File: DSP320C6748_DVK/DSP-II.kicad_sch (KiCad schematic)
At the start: 3 parts, among them IC8 SN74LVC1G11DBVR, U1 TMS320C6748EZWT4

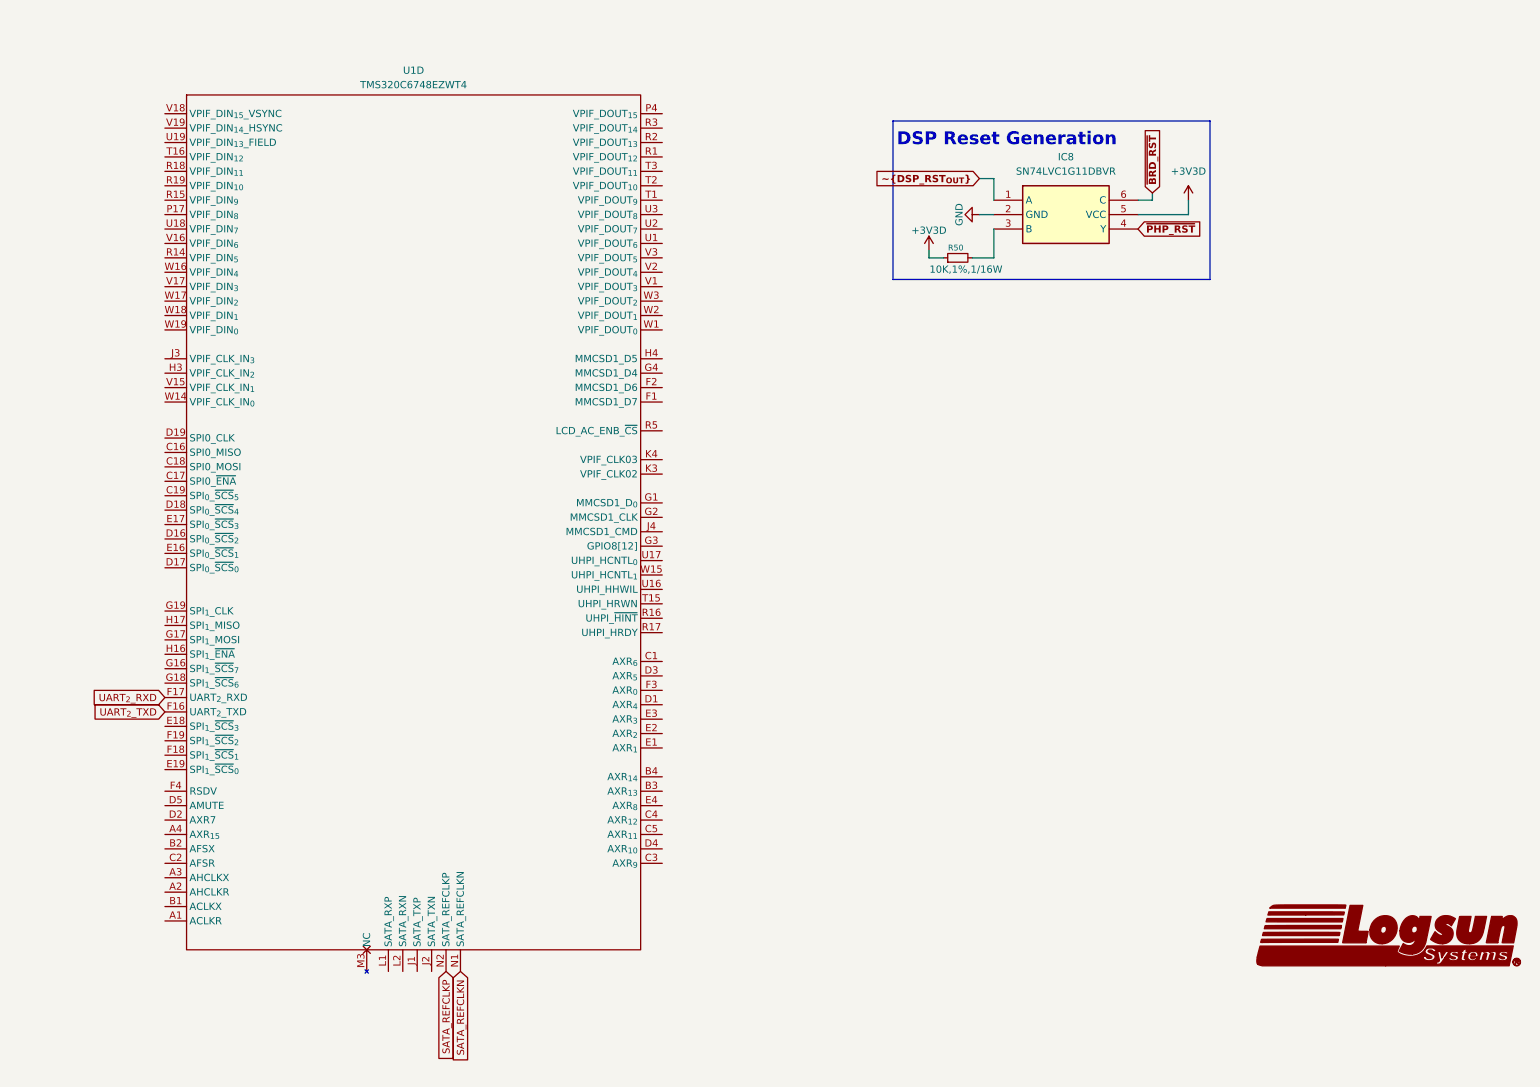
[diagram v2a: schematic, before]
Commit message: Partial VGA-LCD schematic added
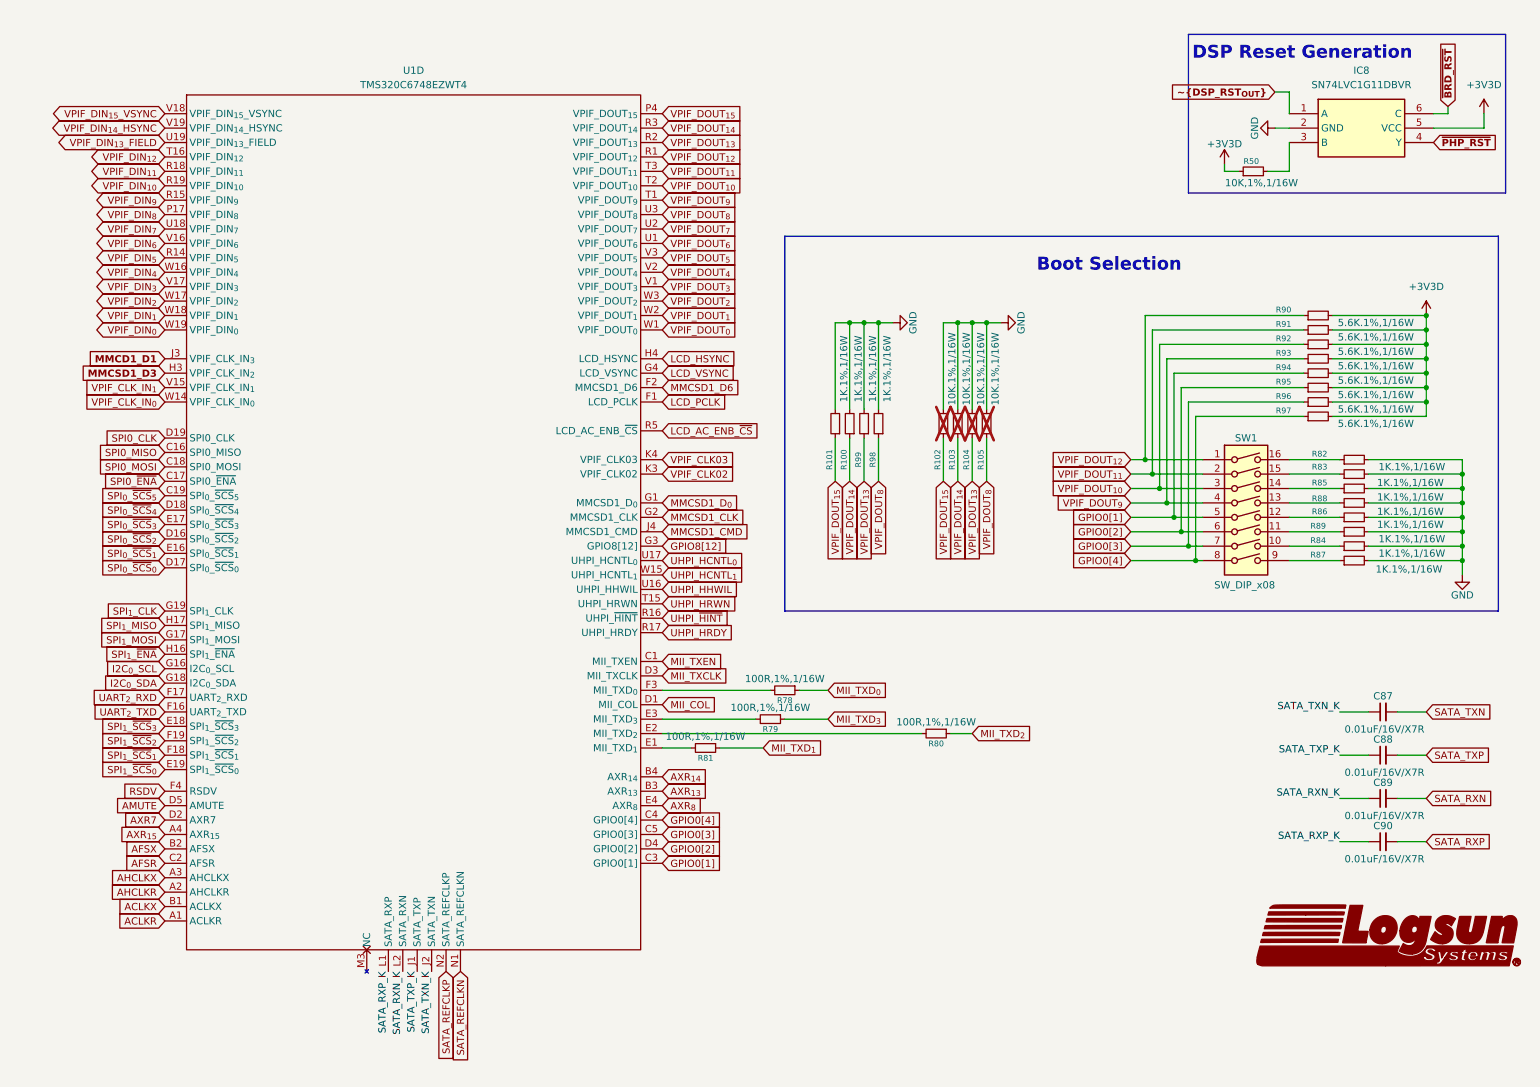
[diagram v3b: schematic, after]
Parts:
- added C87, C88, C89, C90: 0.01uF/16V/X7R, symbol Device:C_Small
- added R100, R101, R82, R83, R84, R85, R86, R87, R88, R89, R98, R99: 1K.1%,1/16W, symbol Device:R_Small
- added R102, R103, R104, R105: 10K.1%,1/16W, symbol Device:R_Small
- added R78, R79, R80, R81: 100R,1%,1/16W, symbol Device:R_Small
- added R90, R91, R92, R93, R94, R95, R96, R97: 5.6K.1%,1/16W, symbol Device:R_Small
- added SW1: SW_DIP_x08, symbol Switch:SW_DIP_x08
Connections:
- net +3V3D: now also R90.2, R91.2, R92.2, R93.2, R94.2, R95.2, R96.2, R97.2
- net GND: now also R100.2, R101.2, R102.2, R103.2, R104.2, R105.2, R82.2, R83.2, R84.2, R85.2, R86.2, R87.2, R88.2, R89.2, R98.2, R99.2
- net ACLKR: now reaches U1.A1 (ACLKR)
- net AHCLKR: now reaches U1.A2 (AHCLKR)
- net AHCLKX: now reaches U1.A3 (AHCLKX)
- net AXR_{15}: now reaches U1.A4 (AXR_{15})
- net ACLKX: now reaches U1.B1 (ACLKX)
- net AFSX: now reaches U1.B2 (AFSX)
- net AXR_{13}: now reaches U1.B3 (AXR_{13})
- net AXR_{14}: now reaches U1.B4 (AXR_{14})
- net MII_TXEN: now reaches U1.C1 (AXR_{6})
- net SPI0_MISO: now reaches U1.C16 (SPI0_MISO)
- net SPI0_~{ENA}: now reaches U1.C17 (SPI0_~{ENA})
- net SPI0_MOSI: now reaches U1.C18 (SPI0_MOSI)
- net SPI_{0}_~{SCS}_{5}: now reaches U1.C19 (SPI_{0}_~{SCS}_{5})
- net AFSR: now reaches U1.C2 (AFSR)
- net GPIO0[1]: now reaches U1.C3 (AXR_{9})
- net GPIO0[1]: now also R94.1, SW1.5
- net GPIO0[4]: now reaches U1.C4 (AXR_{12})
- net GPIO0[4]: now also R97.1, SW1.8
- net GPIO0[3]: now reaches U1.C5 (AXR_{11})
- net GPIO0[3]: now also R96.1, SW1.7
- net MII_COL: now reaches U1.D1 (AXR_{4})
- net SPI_{0}_~{SCS}_{2}: now reaches U1.D16 (SPI_{0}_~{SCS}_{2})
- net SPI_{0}_~{SCS}_{0}: now reaches U1.D17 (SPI_{0}_~{SCS}_{0})
- net SPI_{0}_~{SCS}_{4}: now reaches U1.D18 (SPI_{0}_~{SCS}_{4})
- net SPI0_CLK: now reaches U1.D19 (SPI0_CLK)
- net AXR7: now reaches U1.D2 (AXR7)
- net MII_TXCLK: now reaches U1.D3 (AXR_{5})
- net GPIO0[2]: now reaches U1.D4 (AXR_{10})
- net GPIO0[2]: now also R95.1, SW1.6
- net AMUTE: now reaches U1.D5 (AMUTE)
- net at U1.E1 (AXR_{1}): now also R81.2
- net SPI_{0}_~{SCS}_{1}: now reaches U1.E16 (SPI_{0}_~{SCS}_{1})
- net SPI_{0}_~{SCS}_{3}: now reaches U1.E17 (SPI_{0}_~{SCS}_{3})
- net SPI_{1}_~{SCS}_{3}: now reaches U1.E18 (SPI_{1}_~{SCS}_{3})
- net SPI_{1}_~{SCS}_{0}: now reaches U1.E19 (SPI_{1}_~{SCS}_{0})
- net at U1.E2 (AXR_{2}): now also R80.2
- net at U1.E3 (AXR_{3}): now also R79.2
- net AXR_{8}: now reaches U1.E4 (AXR_{8})
- net LCD_PCLK: now reaches U1.F1 (MMCSD1_D7)
- net SPI_{1}_~{SCS}_{1}: now reaches U1.F18 (SPI_{1}_~{SCS}_{1})
- net SPI_{1}_~{SCS}_{2}: now reaches U1.F19 (SPI_{1}_~{SCS}_{2})
- net MMCSD1_D6: now reaches U1.F2 (MMCSD1_D6)
- net at U1.F3 (AXR_{0}): now also R78.2
- net RSDV: now reaches U1.F4 (RSDV)
- net MMCSD1_D_{0}: now reaches U1.G1 (MMCSD1_D_{0})
- net I2C_{0}_SCL: now reaches U1.G16 (SPI_{1}_~{SCS}_{7})
- net SPI_{1}_MOSI: now reaches U1.G17 (SPI_{1}_MOSI)
- net I2C_{0}_SDA: now reaches U1.G18 (SPI_{1}_~{SCS}_{6})
- net SPI_{1}_CLK: now reaches U1.G19 (SPI_{1}_CLK)
- net MMCSD1_CLK: now reaches U1.G2 (MMCSD1_CLK)
- net GPIO8[12]: now reaches U1.G3 (GPIO8[12])
- net LCD_VSYNC: now reaches U1.G4 (MMCSD1_D4)
- net SPI_{1}_~{ENA}: now reaches U1.H16 (SPI_{1}_~{ENA})
- net SPI_{1}_MISO: now reaches U1.H17 (SPI_{1}_MISO)
- net MMCSD1_D3: now reaches U1.H3 (VPIF_CLK_IN_{2})
- net LCD_HSYNC: now reaches U1.H4 (MMCSD1_D5)
- net SATA_TXP_K: now reaches U1.J1 (SATA_TXP)
- net SATA_TXP_K: now also C88.1
- net SATA_TXN_K: now reaches U1.J2 (SATA_TXN)
- net SATA_TXN_K: now also C87.1
- net MMCD1_D1: now reaches U1.J3 (VPIF_CLK_IN_{3})
- net MMCSD1_CMD: now reaches U1.J4 (MMCSD1_CMD)
- net VPIF_CLK02: now reaches U1.K3 (VPIF_CLK02)
- net VPIF_CLK03: now reaches U1.K4 (VPIF_CLK03)
- net SATA_RXP_K: now reaches U1.L1 (SATA_RXP)
- net SATA_RXP_K: now also C90.1
- net SATA_RXN_K: now reaches U1.L2 (SATA_RXN)
- net SATA_RXN_K: now also C89.1
- net VPIF_DIN_{8}: now reaches U1.P17 (VPIF_DIN_{8})
- net VPIF_DOUT_{15}: now reaches U1.P4 (VPIF_DOUT_{15})
- net VPIF_DOUT_{15}: now also R101.1, R102.1
- net VPIF_DOUT_{12}: now reaches U1.R1 (VPIF_DOUT_{12})
- net VPIF_DOUT_{12}: now also R90.1, SW1.1
- net VPIF_DIN_{5}: now reaches U1.R14 (VPIF_DIN_{5})
- net VPIF_DIN_{9}: now reaches U1.R15 (VPIF_DIN_{9})
- net UHPI_~{HINT}: now reaches U1.R16 (UHPI_~{HINT})
- net UHPI_HRDY: now reaches U1.R17 (UHPI_HRDY)
- net VPIF_DIN_{11}: now reaches U1.R18 (VPIF_DIN_{11})
- net VPIF_DIN_{10}: now reaches U1.R19 (VPIF_DIN_{10})
- net VPIF_DOUT_{13}: now reaches U1.R2 (VPIF_DOUT_{13})
- net VPIF_DOUT_{13}: now also R104.1, R99.1
- net VPIF_DOUT_{14}: now reaches U1.R3 (VPIF_DOUT_{14})
- net VPIF_DOUT_{14}: now also R100.1, R103.1
- net LCD_AC_ENB_~{CS}: now reaches U1.R5 (LCD_AC_ENB_~{CS})
- net VPIF_DOUT_{9}: now reaches U1.T1 (VPIF_DOUT_{9})
- net VPIF_DOUT_{9}: now also R93.1, SW1.4
- net UHPI_HRWN: now reaches U1.T15 (UHPI_HRWN)
- net VPIF_DIN_{12}: now reaches U1.T16 (VPIF_DIN_{12})
- net VPIF_DOUT_{10}: now reaches U1.T2 (VPIF_DOUT_{10})
- net VPIF_DOUT_{10}: now also R92.1, SW1.3
- net VPIF_DOUT_{11}: now reaches U1.T3 (VPIF_DOUT_{11})
- net VPIF_DOUT_{11}: now also R91.1, SW1.2
- net VPIF_DOUT_{6}: now reaches U1.U1 (VPIF_DOUT_{6})
- net UHPI_HHWIL: now reaches U1.U16 (UHPI_HHWIL)
- net UHPI_HCNTL_{0}: now reaches U1.U17 (UHPI_HCNTL_{0})
- net VPIF_DIN_{7}: now reaches U1.U18 (VPIF_DIN_{7})
- net VPIF_DIN_{13}_FIELD: now reaches U1.U19 (VPIF_DIN_{13}_FIELD)
- net VPIF_DOUT_{7}: now reaches U1.U2 (VPIF_DOUT_{7})
- net VPIF_DOUT_{8}: now reaches U1.U3 (VPIF_DOUT_{8})
- net VPIF_DOUT_{8}: now also R105.1, R98.1
- net VPIF_DOUT_{3}: now reaches U1.V1 (VPIF_DOUT_{3})
- net VPIF_CLK_IN_{1}: now reaches U1.V15 (VPIF_CLK_IN_{1})
- net VPIF_DIN_{6}: now reaches U1.V16 (VPIF_DIN_{6})
- net VPIF_DIN_{3}: now reaches U1.V17 (VPIF_DIN_{3})
- net VPIF_DIN_{15}_VSYNC: now reaches U1.V18 (VPIF_DIN_{15}_VSYNC)
- net VPIF_DIN_{14}_HSYNC: now reaches U1.V19 (VPIF_DIN_{14}_HSYNC)
- net VPIF_DOUT_{4}: now reaches U1.V2 (VPIF_DOUT_{4})
- net VPIF_DOUT_{5}: now reaches U1.V3 (VPIF_DOUT_{5})
- net VPIF_DOUT_{0}: now reaches U1.W1 (VPIF_DOUT_{0})
- net VPIF_CLK_IN_{0}: now reaches U1.W14 (VPIF_CLK_IN_{0})
- net UHPI_HCNTL_{1}: now reaches U1.W15 (UHPI_HCNTL_{1})
- net VPIF_DIN_{4}: now reaches U1.W16 (VPIF_DIN_{4})
- net VPIF_DIN_{2}: now reaches U1.W17 (VPIF_DIN_{2})
- net VPIF_DIN_{1}: now reaches U1.W18 (VPIF_DIN_{1})
- net VPIF_DIN_{0}: now reaches U1.W19 (VPIF_DIN_{0})
- net VPIF_DOUT_{1}: now reaches U1.W2 (VPIF_DOUT_{1})
- net VPIF_DOUT_{2}: now reaches U1.W3 (VPIF_DOUT_{2})
- new net: R83.1, SW1.15
- new net: R85.1, SW1.14
- new net: R84.1, SW1.10
- new net: R89.1, SW1.11
- new net: R86.1, SW1.12
- new net: R88.1, SW1.13
- new net: R82.1, SW1.16
- new net: R87.1, SW1.9
- new net MII_TXD_{0}: R78.1
- new net MII_TXD_{1}: R81.1
- new net MII_TXD_{2}: R80.1
- new net MII_TXD_{3}: R79.1
- new net SATA_RXN: C89.2
- new net SATA_RXP: C90.2
- new net SATA_TXN: C87.2
- new net SATA_TXP: C88.2
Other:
- note added: "Boot Selection"
- moved on the sheet: IC8, R50

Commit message: LCD Schematic Completed
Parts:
- added D8, D9: LED_RED, symbol Device:LED_Small
- added IC10, IC11: MUN5211DW1T1G, SOT65P210X110-6N, symbol MUN5211DW1T1G:MUN5211DW1T1G
- added R112: 0R,5%,1/10W, symbol Device:R_Small
- added R113, R114, R115, R116: 10K,1%,1/16W, symbol Device:R_Small
- added R117, R118: 33R,5%,1/16W, symbol Device:R_Small
- added R119, R122: 330R,5%,1/16W, symbol Device:R_Small
- added R120, R121: 100K,5%,1/16W, symbol Device:R_Small
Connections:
- net +3V3D: now also R113.2, R114.2, R115.2, R116.2, R119.1, R122.1
- net ACLKX: now also R117.1
- net AFSX: now also R118.1
- net GND: now also IC10.1 (E2), IC11.1 (E2), R120.2, R121.2
- net I2C_{0}_SCL: now also R113.1
- net I2C_{0}_SDA: now also R114.1
- net UART_{2}_RXD: now also R115.1
- net UART_{2}_TXD: now also R116.1
- net VPIF_CLK_IN_{1}: now also R112.2
- net UHPI_HRDY renamed GPIO6[13]
- net GPIO6[13]: now also IC10.2 (B2), R120.1
- net UHPI_~{HINT} renamed GPIO6[12]
- net GPIO6[12]: now also IC11.2 (B2), R121.1
- net VPIF_CLK_IN_{0} renamed CAM_CLK
- net CAM_CLK: now also R112.1
- new net: D9.1 (K), IC11.6 (C2)
- new net: D9.2 (A), R122.2
- new net: D8.2 (A), R119.2
- new net: D8.1 (K), IC10.6 (C2)
- new net AIC_BCLK: R117.2
- new net AIC_WCLK: R118.2
- no-connect marks 0 -> 6
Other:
- note added: "0111"
- note added: "1010"
- note added: "Bits"
- note added: "Device"
- note added: "NAND Flash"
- note added: "UART2"
- moved on the sheet: R100, R101, R102, R103, R104, R105, R78, R79, R80, R81, R82, R83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

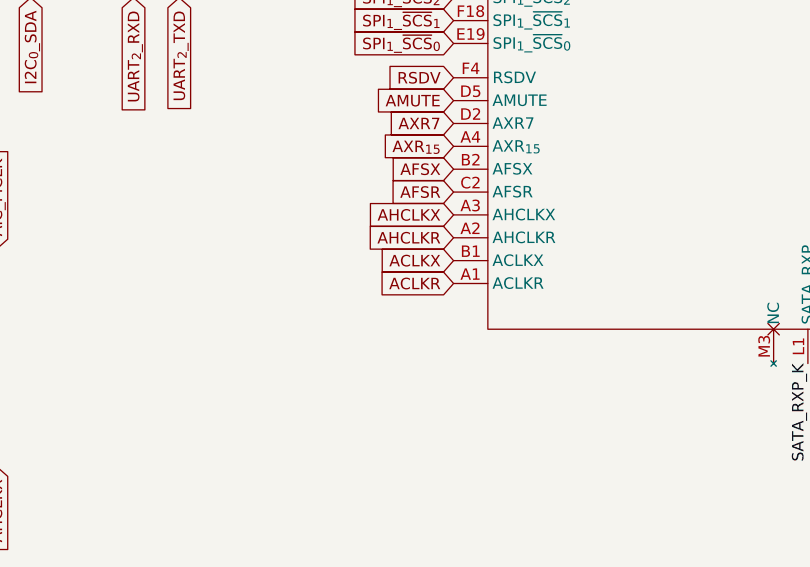
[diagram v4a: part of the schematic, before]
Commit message: Video and Audio Codec Schematic added
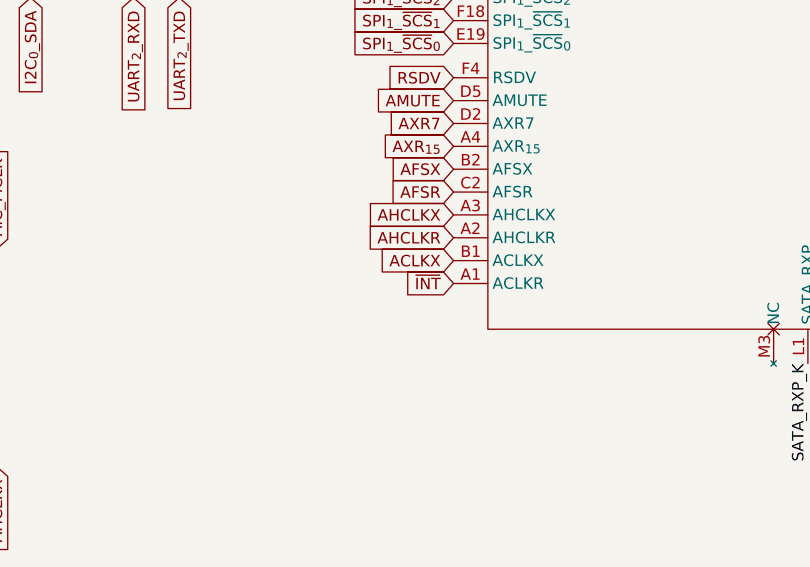
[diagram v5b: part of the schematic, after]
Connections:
- net ACLKR renamed ~{INT}
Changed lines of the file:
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@@
 		)
 	)
-	(global_label "ACLKR"
+	(global_label "~{INT}"
 		(shape input)
 		(at 74.93 166.37 180)

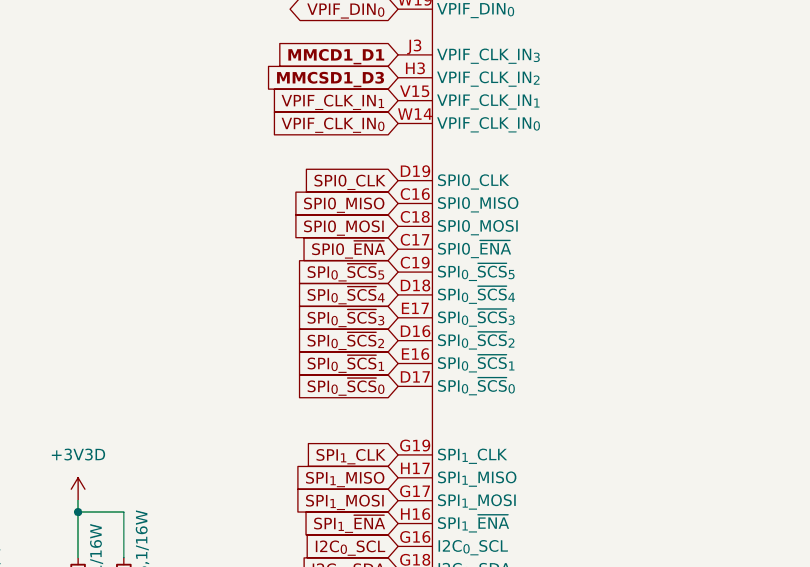
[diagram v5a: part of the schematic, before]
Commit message: LAN Schematic Added
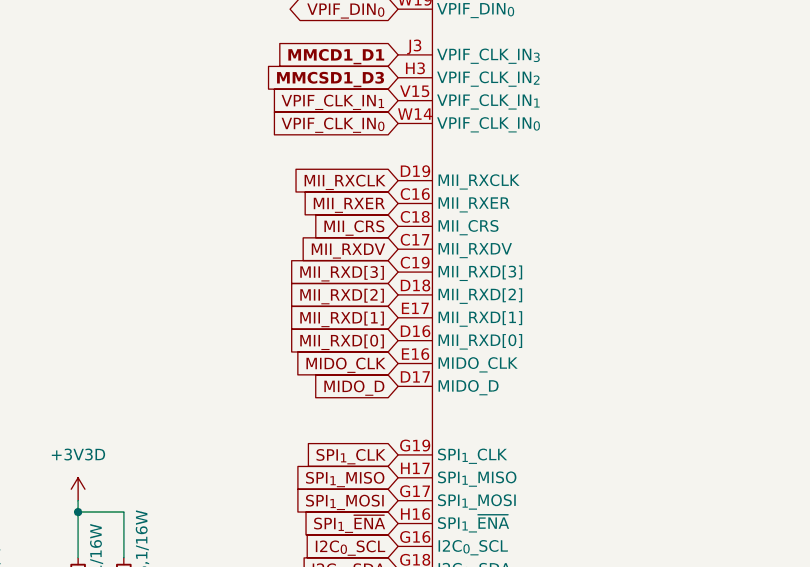
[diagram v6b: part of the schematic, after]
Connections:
- net SPI0_CLK renamed MII_RXCLK
- net SPI0_MISO renamed MII_RXER
- net SPI0_MOSI renamed MII_CRS
- net SPI0_~{ENA} renamed MII_RXDV
- net SPI_{0}_~{SCS}_{0} renamed MIDO_D
- net SPI_{0}_~{SCS}_{1} renamed MIDO_CLK
- net SPI_{0}_~{SCS}_{2} renamed MII_RXD[0]
- net SPI_{0}_~{SCS}_{3} renamed MII_RXD[1]
- net SPI_{0}_~{SCS}_{4} renamed MII_RXD[2]
- net SPI_{0}_~{SCS}_{5} renamed MII_RXD[3]

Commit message: Connectors and mislleneous components added
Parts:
- removed R100, R101, R82, R83, R84, R85, R86, R87, R88, R89, R98, R99: 1K.1%,1/16W, symbol Device:R_Small
- removed R102, R103, R104, R105: 10K.1%,1/16W, symbol Device:R_Small
- removed R90, R91, R92, R93, R94, R95, R96, R97: 5.6K.1%,1/16W, symbol Device:R_Small
- removed SW1: SW_DIP_x08, symbol Switch:SW_DIP_x08
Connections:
- net AMUTE renamed GPIO0[9]
- net MMCSD1_D6 renamed GPIO8[10]
- net RSDV renamed GPIO0[8]
- net SPI_{1}_~{ENA} renamed GPIO2[12]
- net SPI_{1}_~{SCS}_{2} renamed UART_{1}_TXD
- net SPI_{1}_~{SCS}_{3} renamed UART_{1}RXD
- net UHPI_HCNTL_{0} renamed GPIO6[11]
- net UHPI_HCNTL_{1} renamed GPIO6[10]
- net UHPI_HHWIL renamed GPIO6[9]
- net VPIF_CLK02 renamed MMCSD1_D_{2}
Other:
- note removed: "0111"
- note removed: "1010"
- note removed: "Bits"
- note removed: "Boot Selection"
- note removed: "Device"
- note removed: "NAND Flash"
- note removed: "UART2"

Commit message: Whole Schematic Reannotation Done
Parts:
- renumbered C87 to C50, C88 to C51, C89 to C52, C90 to C53, D8 to D1, D9 to D2, IC8 to IC1, IC10 to IC2, IC11 to IC3, R118 to R28, R117 to R29, R112 to R30, R113 to R31, R114 to R32, R115 to R33, R116 to R34, R81 to R35, R79 to R36, R78 to R37, R80 to R38, R50 to R39, R120 to R40, R121 to R41, R119 to R42, R122 to R43
